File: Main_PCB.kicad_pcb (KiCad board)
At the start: 4 copper layers, 178.5 x 70 mm, 78 parts, among them IC1 TCN75AVUA713-VAO, J1 Conn_Coaxial, J2 Conn_02x03_Odd_Even, J3 USB_C_Receptacle_USB2.0, J4 Conn_01x03_Male, J5 Conn_01x08, J6 Conn_01x08, J7 Conn_01x06_Male, SW1 SW_Push, SW2 SW_Push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

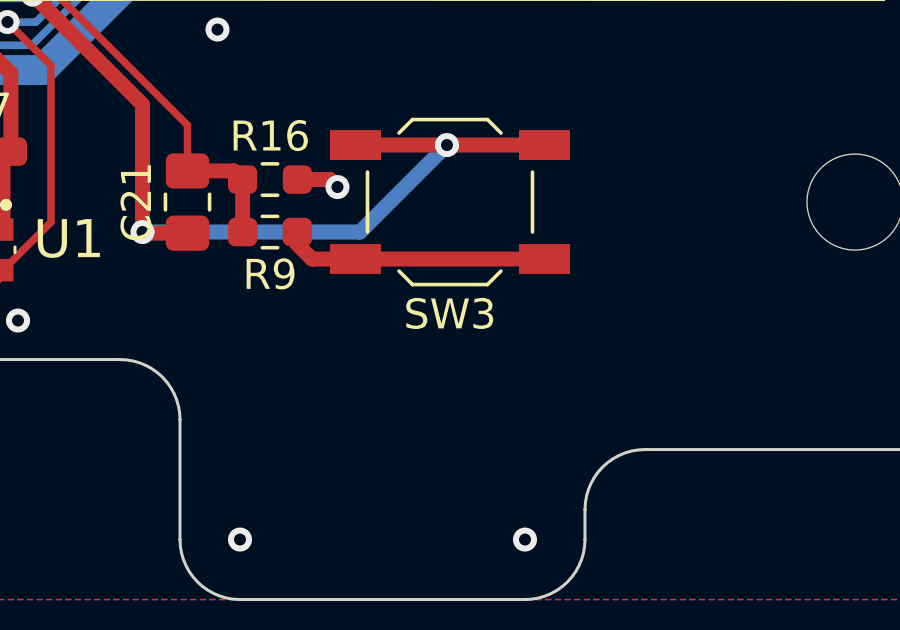
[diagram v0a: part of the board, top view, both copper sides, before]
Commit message: updated ldo
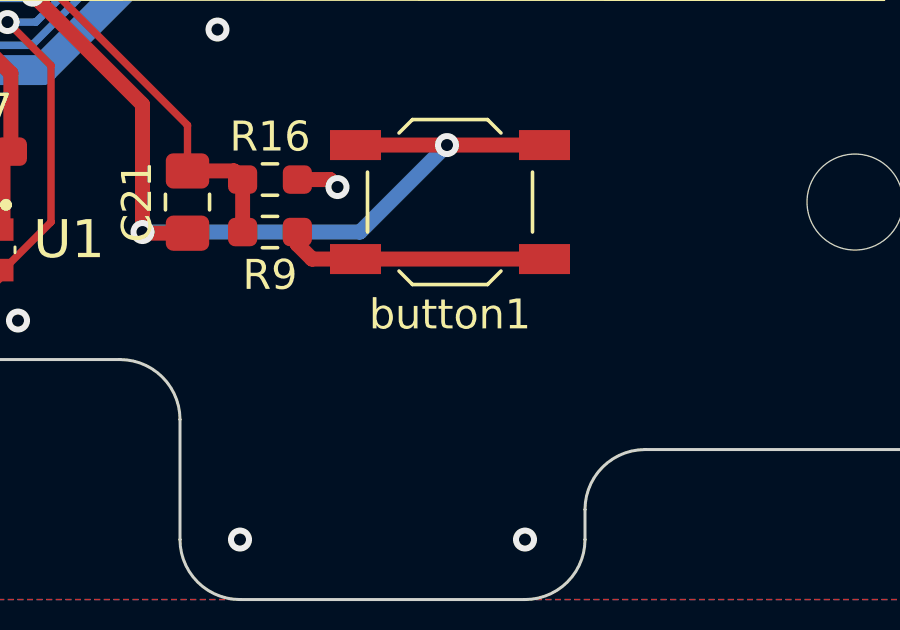
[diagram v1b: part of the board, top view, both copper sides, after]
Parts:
- renumbered SW3 to button1
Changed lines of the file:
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@@
     (property "Sheetname" "")
     (attr smd)
-    (fp_text reference "SW3" (at 0 -3.75) (layer "F.SilkS")
+    (fp_text reference "button1" (at 0 -3.75) (layer "F.SilkS")
       (effects (font (size 1 1) (thickness 0.15)))
     )

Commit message: updated ldo and fixed git mistake
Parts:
- removed PS1: S-1318B33-M5T1U4, S-1318B33:SOT95P275X130-5N
- added R17: 1M, Resistor_SMD:R_0603_1608Metric_Pad0.98x0.95mm_HandSolder, F.Cu at (199.5, 117.8)
- added U9: TC1054, Package_TO_SOT_SMD:SOT-23-5, F.Cu at (199.8, 120.5)
- C13, C17, C18, C19, C2, C20, C21: footprint Capacitor_SMD:C_0805_2012Metric_Pad1.18x1.45mm_HandSolder -> Capacitor_SMD:C_0603_1608Metric_Pad1.08x0.95mm_HandSolder
- C15: value 100nF -> 1uF; footprint Capacitor_SMD:C_0603_1608Metric_Pad1.08x0.95mm_HandSolder -> Capacitor_SMD:C_0805_2012Metric_Pad1.18x1.45mm_HandSolder
- moved C14 3.25 mm to (196.8, 119.5), turned to 90 degrees
- moved R1 1.80 mm to (195.0, 119.5)
- moved C15 1.12 mm to (203.0, 120.5), turned to 90 degrees
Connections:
- U6 pad 26: unconnected-(U6-Pad26) -> /LDO_err
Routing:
- net Net-(R17-Pad1): track 0.00 -> 5.12 mm
- net GND: track 104.1 -> 99.4 mm, vias 114 -> 113
- net Net-(R1-Pad2): track 1.77 -> 4.04 mm
- net VBAT: track 211.6 -> 212.7 mm

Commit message: updated version names
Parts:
- moved C12 0.25 mm to (99.0, 78.0)
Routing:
- net GND: track 99.4 -> 100.1 mm
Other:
- board text added: "Pulu soil monitor v1.2"
- board text removed: "Pulu soil monitor v1.0"
